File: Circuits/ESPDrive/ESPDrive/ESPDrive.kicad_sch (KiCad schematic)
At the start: 51 parts, among them Q1 AOSS32334C, U1 AP63203WU, U2 AP63201WU, U3 LTV-827S

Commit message: Updated ESPDrive Schematic
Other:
- note added: "13.6V Output: 160kΩ 5V Output: 53kΩ"
- note added: "3.3V Output"
- note added: "I/O"
- note added: "Optocouplers"
- note added: "Processor"
- note added: "Relay"
- note added: "Status LED"
- note added: "Voltage Divider"
- note added: "Voltage Regulation"
- moved on the sheet: C1, C10, C11, C12, C15, C16, C2, C3, C4, C6, C7, C8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

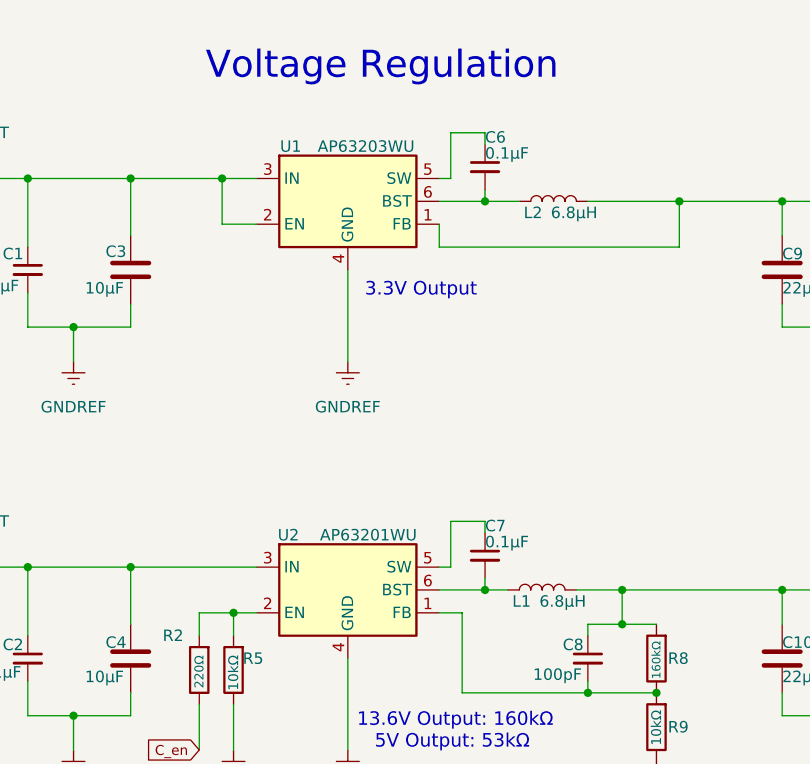
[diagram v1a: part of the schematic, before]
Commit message: ESPDrive: fixed regulator pad errors, small tweaks
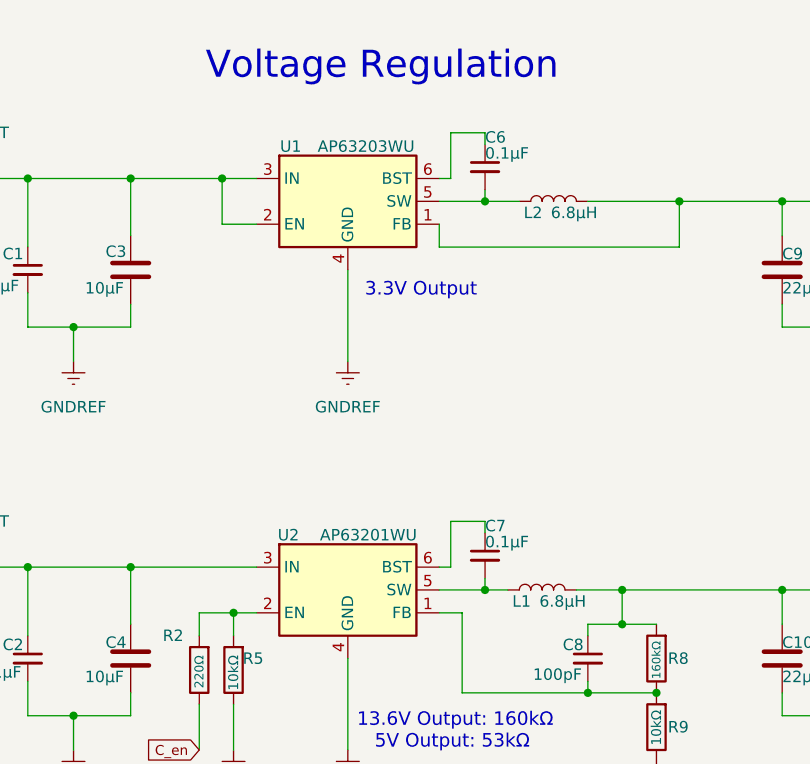
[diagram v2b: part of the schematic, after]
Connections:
- net at C6.2, L2.1: now also U1.5 (SW); no longer U1.6 (BST)
- net at C7.1: now also U2.6 (BST); no longer U2.5 (SW)
- net at C7.2, L1.1: now also U2.5 (SW); no longer U2.6 (BST)
- net at C6.1: now also U1.6 (BST); no longer U1.5 (SW)
